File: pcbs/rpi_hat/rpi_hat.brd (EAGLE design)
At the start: 57.6 x 46.9 mm, 13 parts, among them J2 RJ11-2L-B

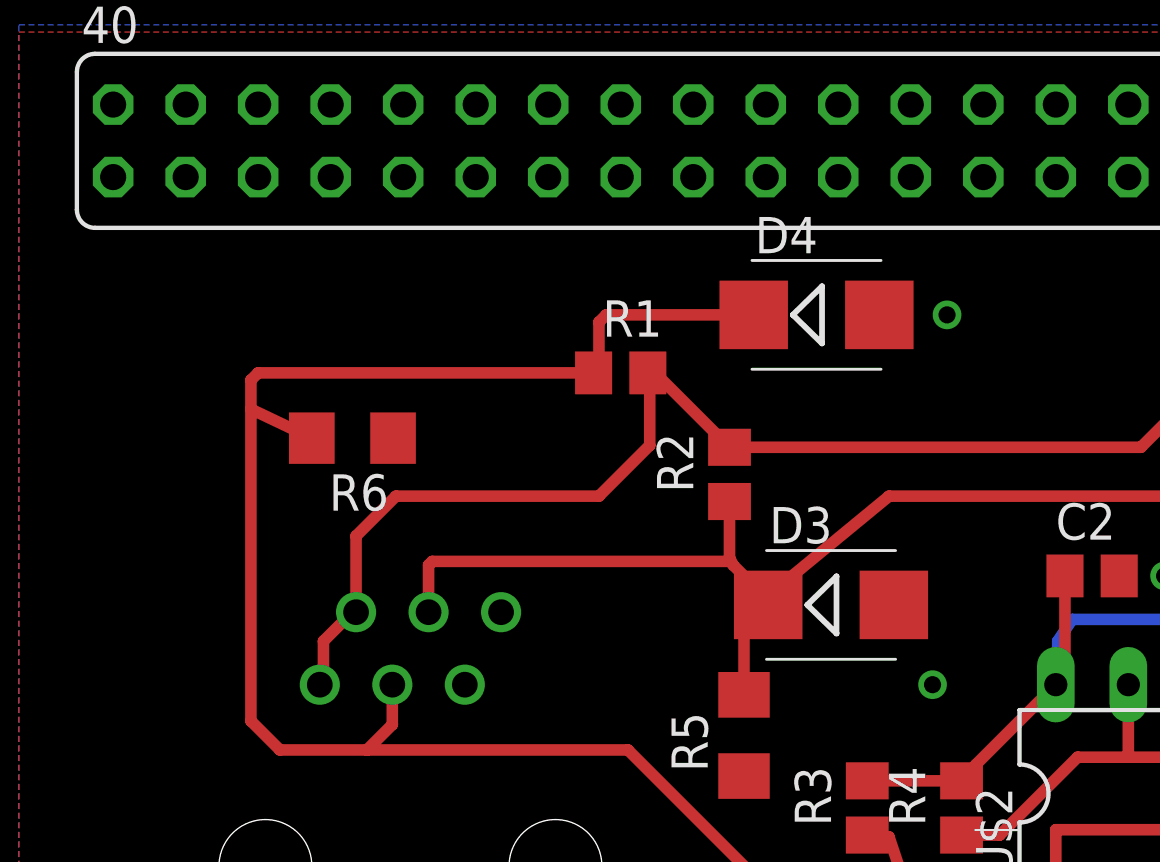
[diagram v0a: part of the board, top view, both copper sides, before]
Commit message: Added the dataready line
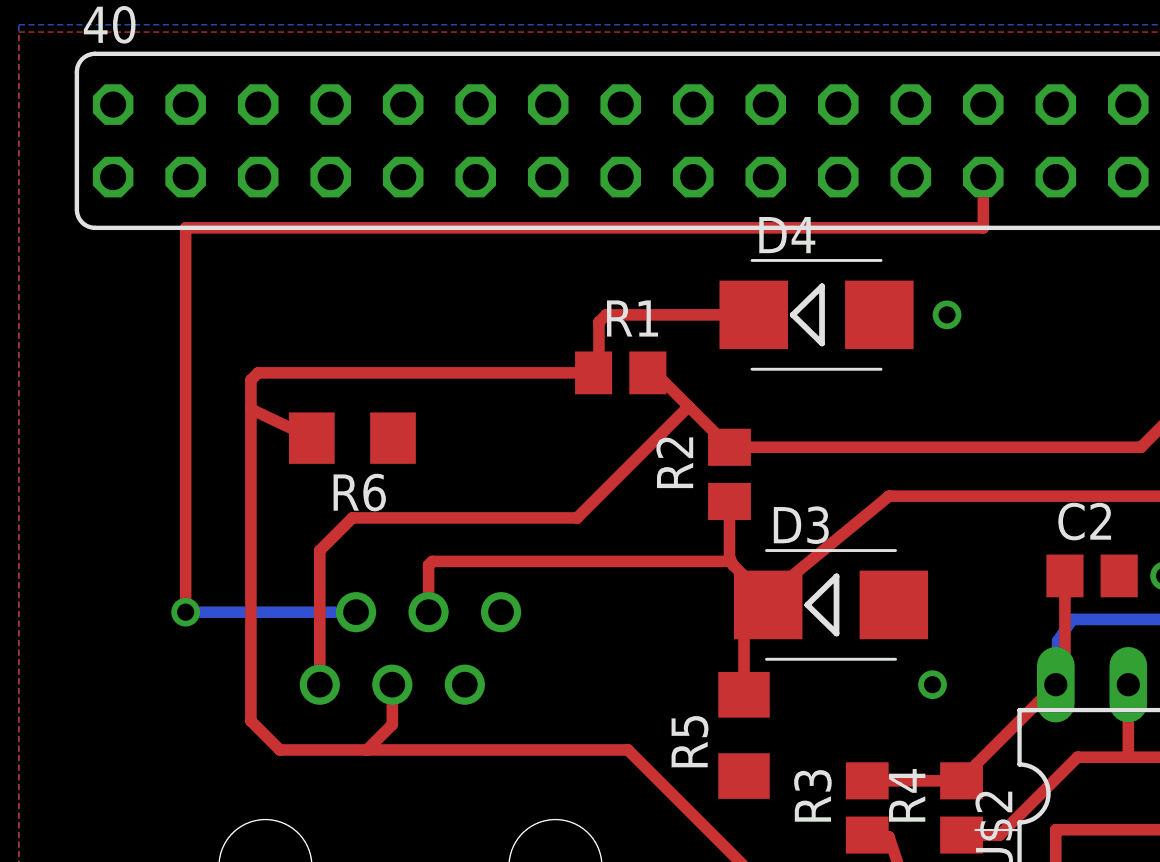
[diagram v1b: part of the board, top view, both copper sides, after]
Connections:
- new net N$3: J2.5, SV1.15
- net N$1: no longer J2.5
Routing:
- net N$3: track 0.00 -> 49.1 mm, vias 0 -> 1
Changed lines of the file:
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@@
 <layer number="14" name="Route14" color="1" fill="6" visible="no" active="no"/>
 <layer number="15" name="Route15" color="4" fill="6" visible="no" active="no"/>
-<layer number="16" name="Bottom" color="1" fill="1" visible="no" active="yes"/>
+<layer number="16" name="Bottom" color="1" fill="1" visible="yes" active="yes"/>
 <layer number="17" name="Pads" color="2" fill="1" visible="yes" active="yes"/>
 <layer number="18" name="Vias" color="2" fill="1" visible="yes" active="yes"/>
@@
 </signal>
 <signal name="N$1">
-<contactref element="J2" pad="5"/>
 <contactref element="R2" pad="2"/>
 <contactref element="J2" pad="6"/>
@@
 <contactref element="C1" pad="1"/>
 <contactref element="SV1" pad="2"/>
-<wire x1="21.59" y1="28.448" x2="23.368" y2="30.226" width="0.4064" layer="1"/>
-<wire x1="23.368" y1="30.226" x2="23.368" y2="32.7" width="0.4064" layer="1"/>
-<wire x1="23.368" y1="32.7" x2="23.302" y2="32.766" width="0.4064" layer="1"/>
 <wire x1="23.302" y1="32.766" x2="23.556" y2="32.766" width="0.4064" layer="1"/>
-<wire x1="23.556" y1="32.766" x2="26.162" y2="30.16" width="0.4064" layer="1"/>
+<wire x1="23.556" y1="32.766" x2="24.732" y2="31.59" width="0.4064" layer="1"/>
+<wire x1="24.732" y1="31.59" x2="26.162" y2="30.16" width="0.4064" layer="1"/>
 <wire x1="26.162" y1="30.16" x2="40.574" y2="30.16" width="0.4064" layer="1"/>
 <wire x1="40.574" y1="30.16" x2="44.958" y2="34.544" width="0.4064" layer="1"/>
@@
 <wire x1="51.562" y1="35.56" x2="51.562" y2="40.894" width="0.4064" layer="1"/>
 <wire x1="51.562" y1="40.894" x2="52.832" y2="42.164" width="0.4064" layer="1"/>
-<wire x1="13.081" y1="24.384" x2="12.954" y2="24.384" width="0.4064" layer="1"/>
-<wire x1="12.954" y1="24.384" x2="11.938" y2="23.368" width="0.4064" layer="1"/>
-<wire x1="11.938" y1="23.368" x2="11.938" y2="21.971" width="0.4064" layer="1"/>
-<wire x1="11.938" y1="21.971" x2="11.811" y2="21.844" width="0.4064" layer="1"/>
-<wire x1="13.081" y1="24.384" x2="13.081" y2="27.051" width="0.4064" layer="1"/>
-<wire x1="13.081" y1="27.051" x2="14.478" y2="28.448" width="0.4064" layer="1"/>
-<wire x1="14.478" y1="28.448" x2="21.59" y2="28.448" width="0.4064" layer="1"/>
+<wire x1="11.811" y1="21.844" x2="11.811" y2="26.543" width="0.4064" layer="1"/>
+<wire x1="11.811" y1="26.543" x2="12.954" y2="27.686" width="0.4064" layer="1"/>
+<wire x1="12.954" y1="27.686" x2="20.828" y2="27.686" width="0.4064" layer="1"/>
+<wire x1="20.828" y1="27.686" x2="24.732" y2="31.59" width="0.4064" layer="1"/>
 </signal>
 <signal name="N$2">
@@
 <wire x1="26.67" y1="21.488" x2="26.67" y2="24.13" width="0.4064" layer="1"/>
 </signal>
+<signal name="N$3">
+<contactref element="J2" pad="5"/>
+<contactref element="SV1" pad="15"/>
+<wire x1="35.052" y1="39.624" x2="35.052" y2="37.846" width="0.4064" layer="1"/>
+<wire x1="35.052" y1="37.846" x2="7.112" y2="37.846" width="0.4064" layer="1"/>
+<wire x1="7.112" y1="37.846" x2="7.112" y2="24.384" width="0.4064" layer="1"/>
+<via x="7.112" y="24.384" extent="1-16" drill="0.6" shape="square"/>
+<wire x1="7.112" y1="24.384" x2="13.081" y2="24.384" width="0.4064" layer="16"/>
+</signal>
 </signals>
